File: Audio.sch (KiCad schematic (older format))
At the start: 42 parts, among them J2 Line in, J3 Line out, U2 vs1053b, U3 MAX9723-TQFN, Y2 12,288MHz

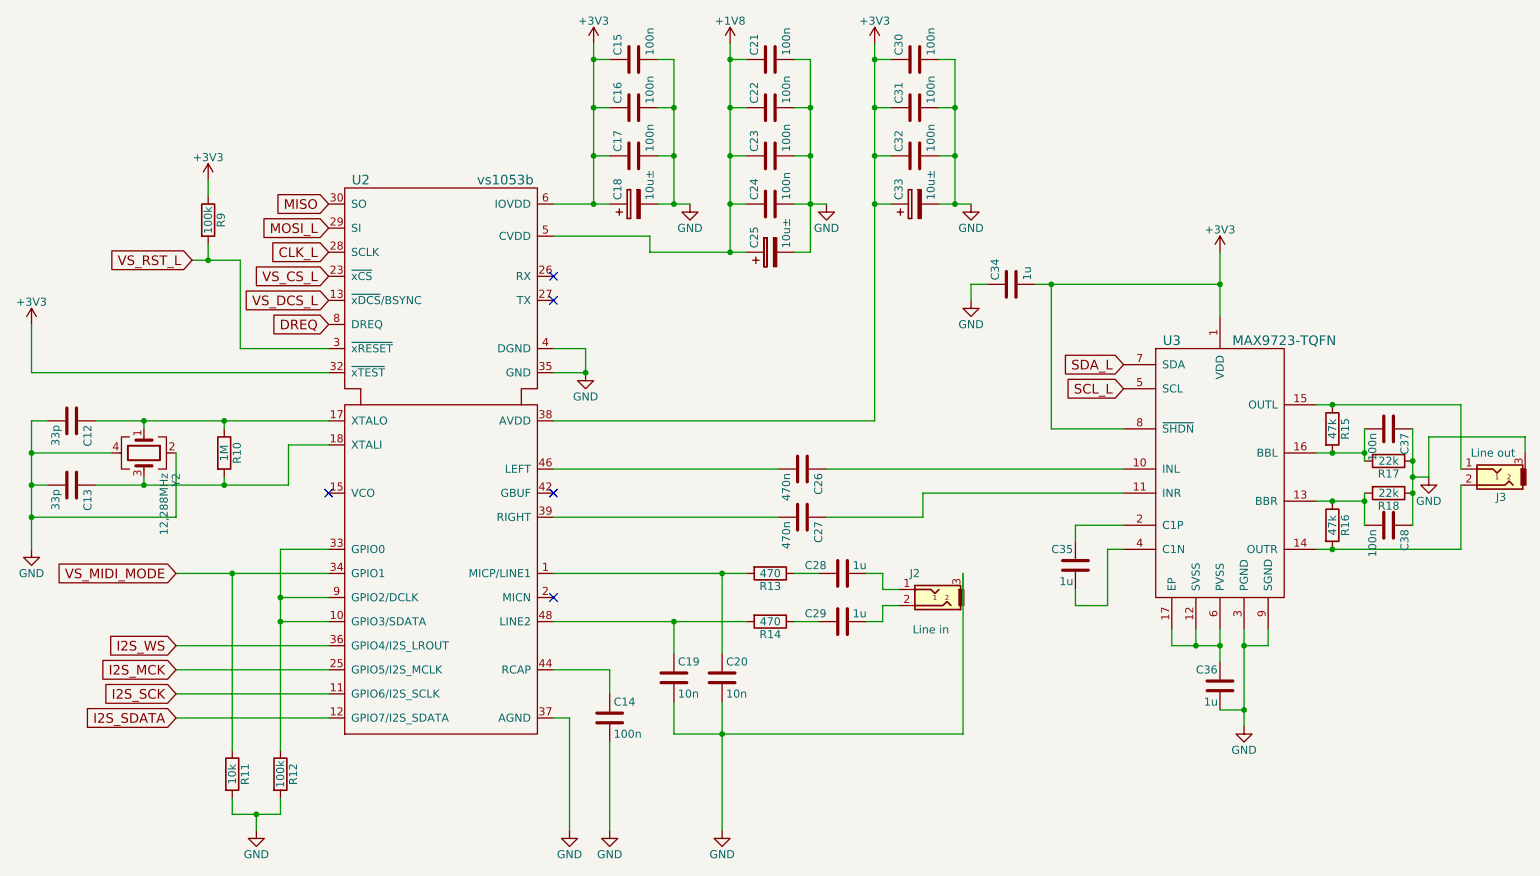
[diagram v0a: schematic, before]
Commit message: Board should be ok. Bargraph leds yet to do.
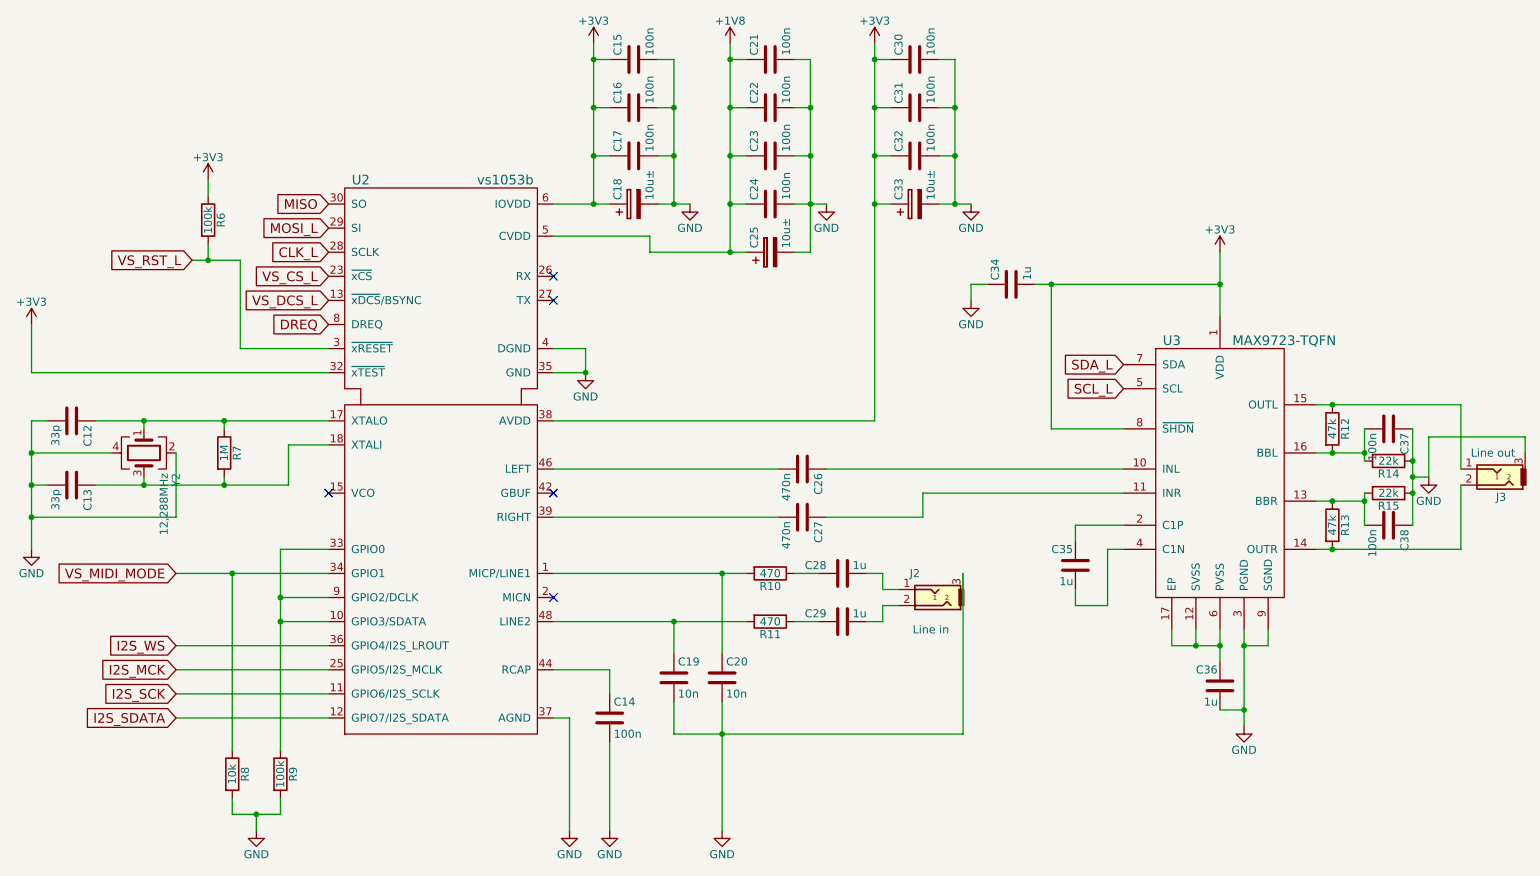
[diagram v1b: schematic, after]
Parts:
- renumbered R13 to R10, R14 to R11, R15 to R12, R16 to R13, R17 to R14, R18 to R15, R9 to R6, R10 to R7, R11 to R8, R12 to R9
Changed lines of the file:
@@
 $EndComp
 $Comp
-L R R10
+L R R7
 U 1 1 59AD1DE0
 P 1950 3400
-F 0 "R10" V 2030 3400 50  0000 C CNN
+F 0 "R7" V 2030 3400 50  0000 C CNN
 F 1 "1M" V 1950 3400 50  0000 C CNN
 F 2 "Resistors_SMD:R_0603" V 1880 3400 50  0001 C CNN
@@
 $EndComp
 $Comp
-L R R13
+L R R10
 U 1 1 59ADC3F0
 P 5350 4150
-F 0 "R13" V 5430 4150 50  0000 C CNN
+F 0 "R10" V 5430 4150 50  0000 C CNN
 F 1 "470" V 5350 4150 50  0000 C CNN
 F 2 "Resistors_SMD:R_0603" V 5280 4150 50  0001 C CNN
@@
 $EndComp
 $Comp
-L R R14
+L R R11
 U 1 1 59ADCA1B
 P 5350 4450
-F 0 "R14" V 5430 4450 50  0000 C CNN
+F 0 "R11" V 5430 4450 50  0000 C CNN
 F 1 "470" V 5350 4450 50  0000 C CNN
 F 2 "Resistors_SMD:R_0603" V 5280 4450 50  0001 C CNN
@@
 $EndComp
 $Comp
-L R R12
+L R R9
 U 1 1 59AE6757
 P 2300 5400
-F 0 "R12" V 2380 5400 50  0000 C CNN
+F 0 "R9" V 2380 5400 50  0000 C CNN
 F 1 "100k" V 2300 5400 50  0000 C CNN
 F 2 "Resistors_SMD:R_0603" V 2230 5400 50  0001 C CNN
@@
 $EndComp
 $Comp
-L R R11
+L R R8
 U 1 1 59AE6A9C
 P 2000 5400
-F 0 "R11" V 2080 5400 50  0000 C CNN
+F 0 "R8" V 2080 5400 50  0000 C CNN
 F 1 "10k" V 2000 5400 50  0000 C CNN
 F 2 "Resistors_SMD:R_0603" V 1930 5400 50  0001 C CNN
@@
 VS_RST_L
 $Comp
-L R R9
+L R R6
 U 1 1 59AEA852
 P 1850 1950
-F 0 "R9" V 1930 1950 50  0000 C CNN
+F 0 "R6" V 1930 1950 50  0000 C CNN
 F 1 "100k" V 1850 1950 50  0000 C CNN
 F 2 "Resistors_SMD:R_0603" V 1780 1950 50  0001 C CNN
@@
 $EndComp
 $Comp
-L R R15
+L R R12
 U 1 1 59AF6C34
 P 8850 3250
-F 0 "R15" V 8930 3250 50  0000 C CNN
+F 0 "R12" V 8930 3250 50  0000 C CNN
 F 1 "47k" V 8850 3250 50  0000 C CNN
 F 2 "Resistors_SMD:R_0603" V 8780 3250 50  0001 C CNN
@@
 $EndComp
 $Comp
-L R R16
+L R R13
 U 1 1 59AF6E11
 P 8850 3850
-F 0 "R16" V 8930 3850 50  0000 C CNN
+F 0 "R13" V 8930 3850 50  0000 C CNN
 F 1 "47k" V 8850 3850 50  0000 C CNN
 F 2 "Resistors_SMD:R_0603" V 8780 3850 50  0001 C CNN
@@
 $EndComp
 $Comp
-L R R17
+L R R14
 U 1 1 59AF74A1
 P 9200 3450
-F 0 "R17" V 9280 3450 50  0000 C CNN
+F 0 "R14" V 9280 3450 50  0000 C CNN
 F 1 "22k" V 9200 3450 50  0000 C CNN
 F 2 "Resistors_SMD:R_0603" V 9130 3450 50  0001 C CNN
@@
 $EndComp
 $Comp
-L R R18
+L R R15
 U 1 1 59AF78F8
 P 9200 3650
-F 0 "R18" V 9280 3650 50  0000 C CNN
+F 0 "R15" V 9280 3650 50  0000 C CNN
 F 1 "22k" V 9200 3650 50  0000 C CNN
 F 2 "Resistors_SMD:R_0603" V 9130 3650 50  0001 C CNN

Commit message: Board modified after ckecking. Ready for fab, just need to create gerber, position and components files.
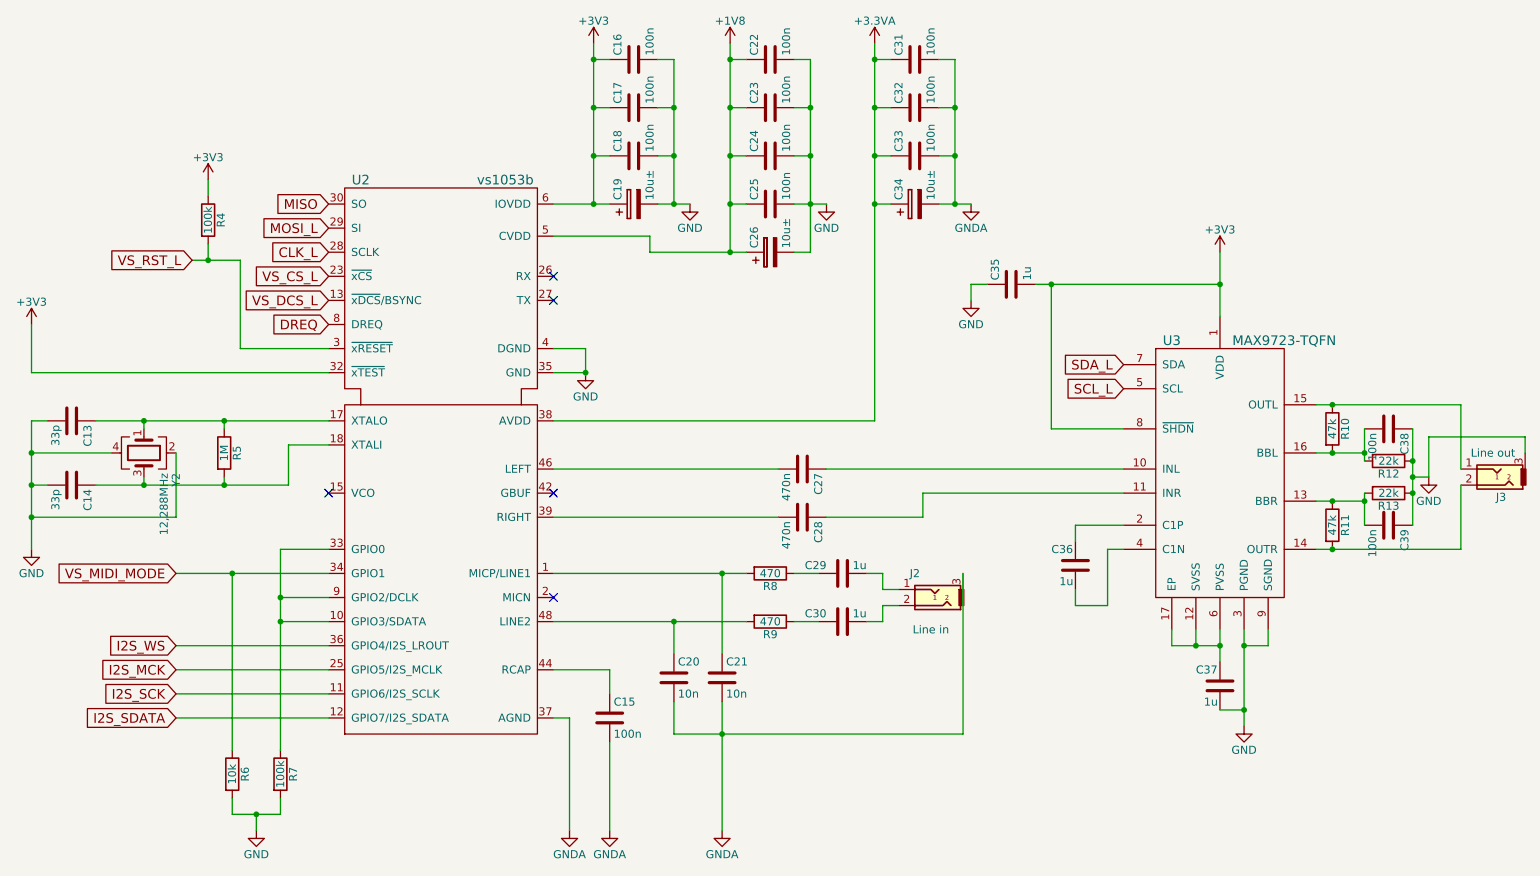
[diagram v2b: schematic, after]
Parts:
- renumbered C12 to C13, C13 to C14, C14 to C15, C15 to C16, C16 to C17, C17 to C18, C18 to C19, C19 to C20, C20 to C21, C21 to C22, C22 to C23, C23 to C24, C24 to C25, C25 to C26, C26 to C27, C27 to C28, C28 to C29, C29 to C30, C30 to C31, C31 to C32, C32 to C33, C33 to C34, C34 to C35, C35 to C36, C36 to C37, C37 to C38, C38 to C39, R12 to R10, R13 to R11, R14 to R12, R15 to R13, R6 to R4, R7 to R5, R8 to R6, R9 to R7, R10 to R8, R11 to R9
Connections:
- net +3V3: no longer C31.1, C32.1, C33.1, C34.1, U2.38 (AVDD), U2.43 (AVDD), U2.45 (AVDD)
- net AGND: no longer C13.2, C14.2, C16.2, C17.2, C18.2, C19.2, C22.2, C23.2, C24.2, C25.2, C26.2, C35.1, C37.2, C38.1, C39.1, J3.3, R12.1, R13.1, R6.2, R7.2, U2.16 (DGND), U2.20 (DGND), U2.21 (DGND), U2.22 (DGND), U2.35 (GND), U2.4 (DGND), U3.3 (PGND), U3.9 (SGND), Y2.2, Y2.4
- new net +3.3VA: C31.1, C32.1, C33.1, C34.1, U2.38 (AVDD), U2.43 (AVDD), U2.45 (AVDD)
- new net DGND: C13.2, C14.2, C16.2, C17.2, C18.2, C19.2, C22.2, C23.2, C24.2, C25.2, C26.2, C35.1, C37.2, C38.1, C39.1, J3.3, R12.1, R13.1, R6.2, R7.2, U2.16 (DGND), U2.20 (DGND), U2.21 (DGND), U2.22 (DGND), U2.35 (GND), U2.4 (DGND), U3.3 (PGND), U3.9 (SGND), Y2.2, Y2.4
